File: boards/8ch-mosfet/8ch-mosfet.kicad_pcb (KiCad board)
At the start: 2 copper layers, 184 x 136 mm, 146 parts, among them J1 N2K, J10 Screw_Terminal_01x02, J11 Screw_Terminal_01x02, J12 Screw_Terminal_01x02, J2 I2C, J3 Screw_Terminal_01x09, J5 Screw_Terminal_01x02, J6 Screw_Terminal_01x02, J7 Screw_Terminal_01x02, J8 Screw_Terminal_01x02, J9 Screw_Terminal_01x02, M1 Fan_4pin, Q1 BC817, Q10 IRF4905, Q11 BC817, Q12 IRF4905, Q13 BC817, Q14 IRF4905, Q15 BC817, Q16 IRF4905, Q2 IRF4905, Q3 BC817, Q4 IRF4905, Q5 BC817, Q6 IRF4905, Q7 BC817, Q8 IRF4905, Q9 BC817, U1 ESP32-DEVKITC, U10 ACS725xLCTR-20AU, U11 ACS725xLCTR-20AU, U12 ACS725xLCTR-20AU, U2 MCP3208, U3 R-78B3.3-2.0, U5 ACS725xLCTR-20AU, U6 ACS725xLCTR-20AU, U7 ACS725xLCTR-20AU, U8 ACS725xLCTR-20AU, U9 ACS725xLCTR-20AU

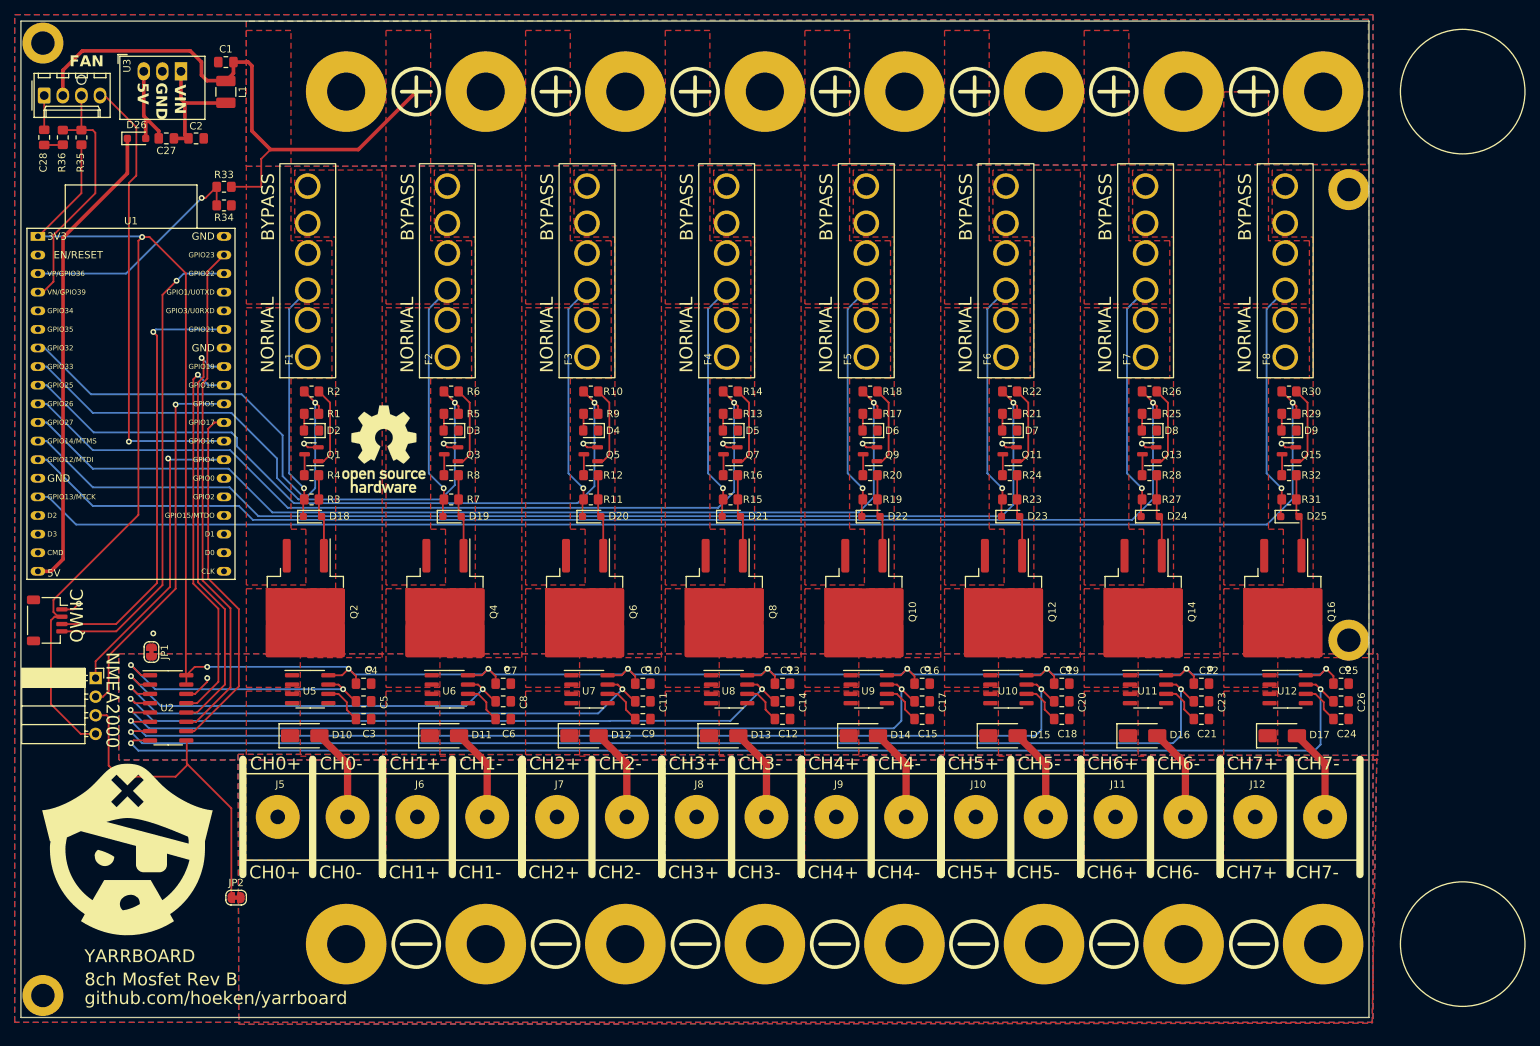
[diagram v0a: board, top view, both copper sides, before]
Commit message: changed ground connectors and updated busbar positions.
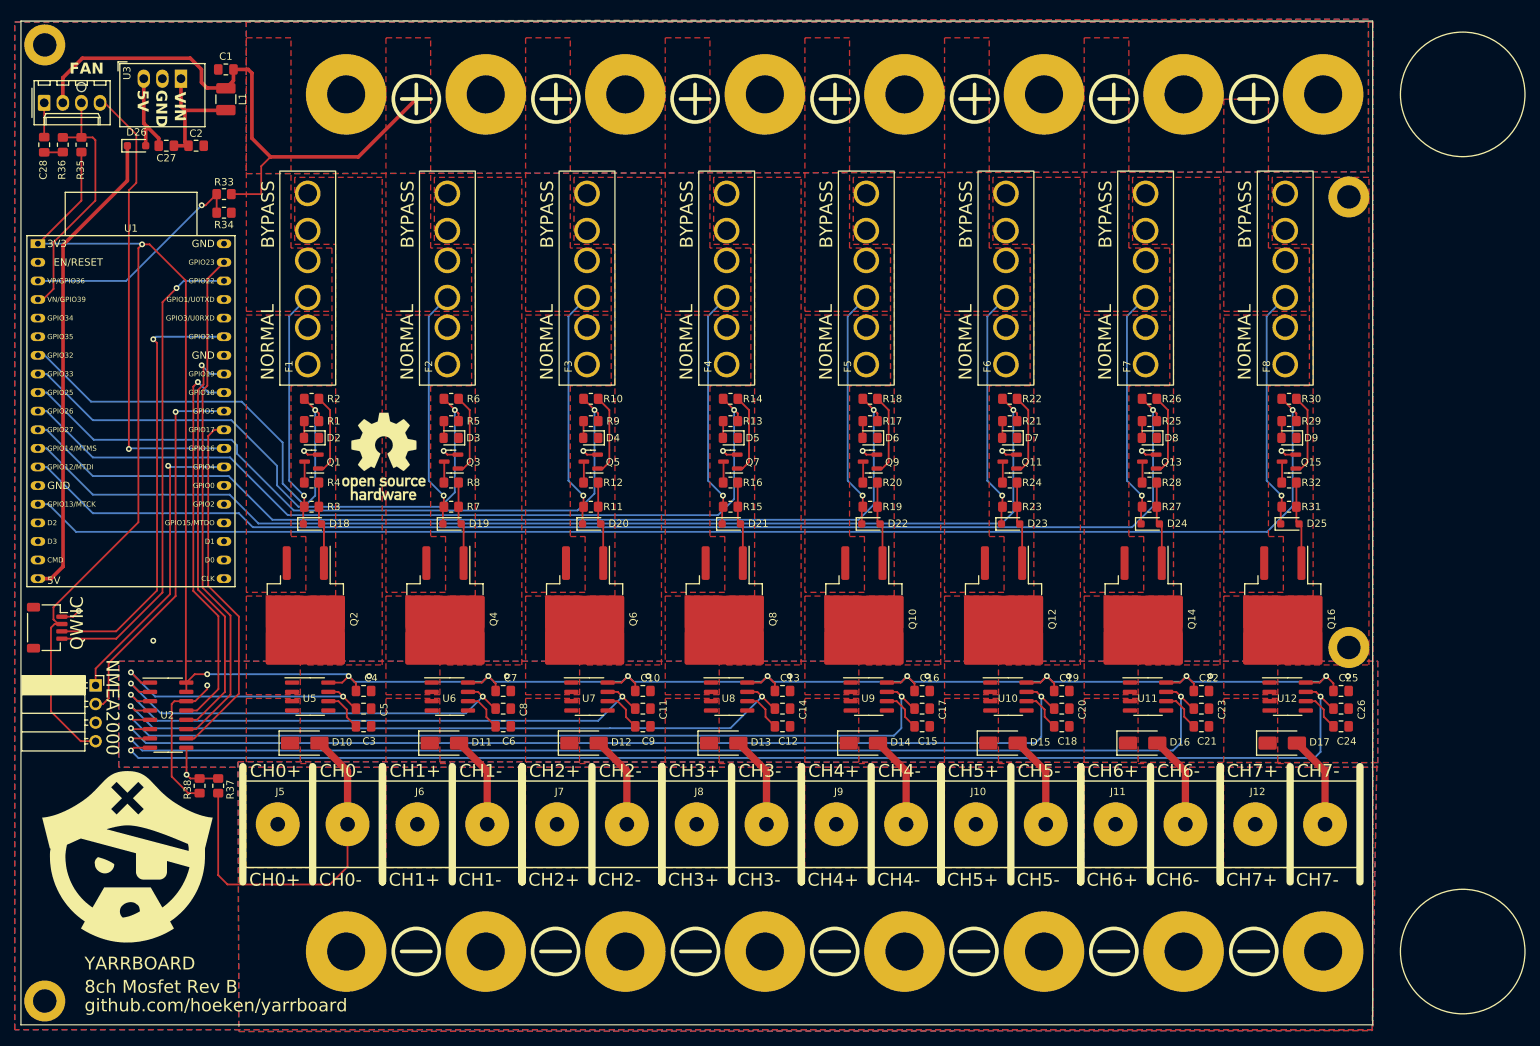
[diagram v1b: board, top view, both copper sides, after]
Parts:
- removed JP1, JP2: SolderJumper_2_Bridged, Jumper:SolderJumper-2_P1.3mm_Bridged_RoundedPad1.0x1.5mm
- added R37: 0R, Resistor_SMD:R_0805_2012Metric_Pad1.20x1.40mm_HandSolder, F.Cu at (26.9, 104.4)
- added R38: 0R, Resistor_SMD:R_0805_2012Metric_Pad1.20x1.40mm_HandSolder, F.Cu at (24.4, 104.4)
- moved locked 1.02 mm to (206.3, 127.0)
- moved C1 1.00 mm to (28.0, 6.60)
- moved C10 1.00 mm to (84.9, 91.4)
- moved C11 1.00 mm to (84.9, 93.8)
- moved C12 1.00 mm to (103.9, 96.3)
- moved C13 1.00 mm to (103.9, 91.4)
- moved C14 1.00 mm to (103.9, 93.8)
- moved C15 1.00 mm to (123.0, 96.3)
- moved C16 1.00 mm to (123.0, 91.4)
- moved C17 1.00 mm to (123.0, 93.8)
- moved C18 1.00 mm to (142.1, 96.3)
- moved C19 1.00 mm to (142.1, 91.4)
- moved C2 1.00 mm to (23.9, 17.0)
- moved C20 1.00 mm to (142.1, 93.8)
- moved C21 1.00 mm to (161.1, 96.3)
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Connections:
- C27 pad 2: Net-(D26-A) -> +5V
- D26 pad 1: +5V -> Net-(D26-K)
- D26 pad 2: Net-(D26-A) -> +5V
- U1 pad 19: +5V -> Net-(D26-K)
- U3 pad 3: Net-(D26-A) -> +5V
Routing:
- net Net-(D26-K): track 0.00 -> 65.2 mm
- net +5V: track 65.2 -> 12.6 mm
- net GNDD: track 69.2 -> 32.9 mm, vias 10 -> 11
- net GNDPWR: track 101.4 -> 137.5 mm
- net GNDA: track 4.23 -> 21.0 mm
- net Net-(D26-A): track 12.6 -> 0.00 mm
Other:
- board size 184 x 136 mm -> 184.5 x 137 mm

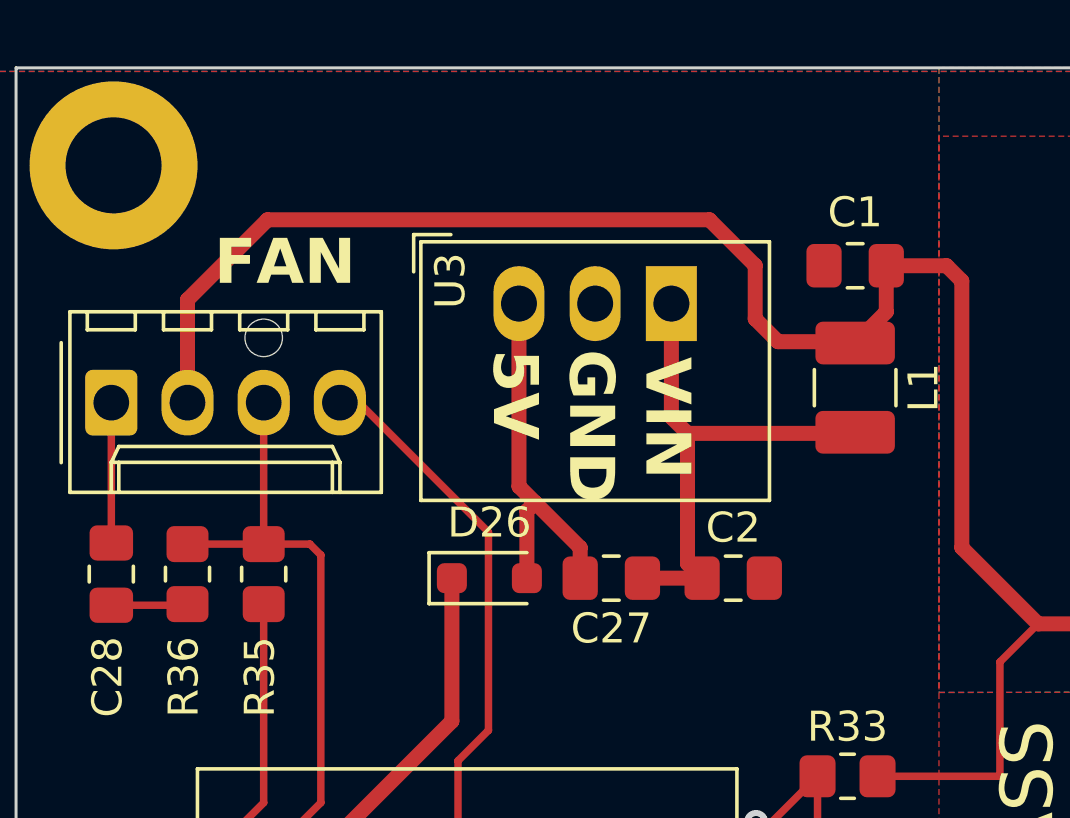
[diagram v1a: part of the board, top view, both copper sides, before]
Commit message: updated footprints, changed 5v diode, and added jumpers for fan voltage
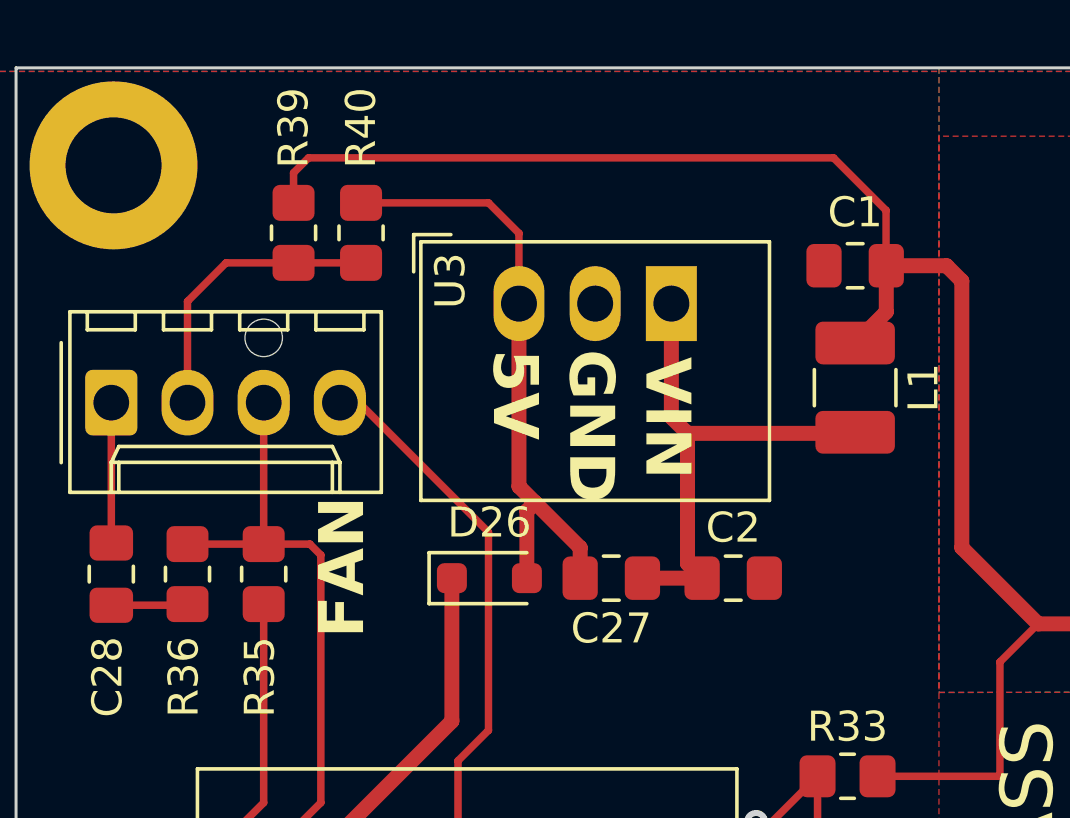
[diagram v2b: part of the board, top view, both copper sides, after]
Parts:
- added R39: 0R, Resistor_SMD:R_0805_2012Metric_Pad1.20x1.40mm_HandSolder, F.Cu at (9.25, 5.50)
- added R40: 0R, Resistor_SMD:R_0805_2012Metric_Pad1.20x1.40mm_HandSolder, F.Cu at (11.5, 5.50)
- D26: value BZX384 -> CMHSH5-2L
- J3, locked: value Screw_Terminal_01x09 -> Screw_Terminal_01x08
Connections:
- M1 pad 2: +24V -> Net-(M1-+)
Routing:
- net Net-(M1-+): track 0.00 -> 9.69 mm
- net +5V: track 12.6 -> 20.7 mm
- net +24V: track 345.5 -> 339.5 mm

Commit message: mosfet driver resistors updated, looking good now.
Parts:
- R11, R15, R19, R23, R27, R3, R31, R7: value 22k -> 100K
- R12, R16, R20, R24, R28, R32, R4, R8: value 4.7k -> 22K
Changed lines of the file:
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@@
         (effects (font (size 1 1) (thickness 0.15)))
     )
-    (fp_text value "22k" (at 0 1.65) (layer "F.Fab")
+    (fp_text value "100K" (at 0 1.65) (layer "F.Fab")
         (effects (font (size 1 1) (thickness 0.15)))
     )
@@
         (effects (font (size 1 1) (thickness 0.15)))
     )
-    (fp_text value "22k" (at 0 1.65) (layer "F.Fab")
+    (fp_text value "100K" (at 0 1.65) (layer "F.Fab")
         (effects (font (size 1 1) (thickness 0.15)))
     )
@@
         (effects (font (size 1 1) (thickness 0.15)))
     )
-    (fp_text value "4.7k" (at 0 1.65) (layer "F.Fab")
+    (fp_text value "22K" (at 0 1.65) (layer "F.Fab")
         (effects (font (size 1 1) (thickness 0.15)))
     )
@@
         (effects (font (size 1 1) (thickness 0.15)))
     )
-    (fp_text value "4.7k" (at 0 1.65) (layer "F.Fab")
+    (fp_text value "22K" (at 0 1.65) (layer "F.Fab")
         (effects (font (size 1 1) (thickness 0.15)))
     )
@@
         (effects (font (size 1 1) (thickness 0.15)))
     )
-    (fp_text value "4.7k" (at 0 1.65) (layer "F.Fab")
+    (fp_text value "22K" (at 0 1.65) (layer "F.Fab")
         (effects (font (size 1 1) (thickness 0.15)))
     )
@@
         (effects (font (size 1 1) (thickness 0.15)))
     )
-    (fp_text value "4.7k" (at 0 1.65) (layer "F.Fab")
+    (fp_text value "22K" (at 0 1.65) (layer "F.Fab")
         (effects (font (size 1 1) (thickness 0.15)))
     )
@@
         (effects (font (size 1 1) (thickness 0.15)))
     )
-    (fp_text value "4.7k" (at 0 1.65) (layer "F.Fab")
+    (fp_text value "22K" (at 0 1.65) (layer "F.Fab")
         (effects (font (size 1 1) (thickness 0.15)))
     )
@@
     (property "Sheetname" "")
     (property "Vendor" " 652-CR0805JW-102ELF ")
+    (property "dnp" "")
     (property "ki_description" "Resistor, small US symbol")
     (property "ki_keywords" "r resistor")
@@
         (effects (font (size 1 1) (thickness 0.15)))
     )
-    (fp_text value "22k" (at 0 1.65) (layer "F.Fab")
+    (fp_text value "100K" (at 0 1.65) (layer "F.Fab")
         (effects (font (size 1 1) (thickness 0.15)))
     )
@@
         (effects (font (size 1 1) (thickness 0.15)))
     )
-    (fp_text value "22k" (at 0 1.65) (layer "F.Fab")
+    (fp_text value "100K" (at 0 1.65) (layer "F.Fab")
         (effects (font (size 1 1) (thickness 0.15)))
     )
@@
         (effects (font (size 1 1) (thickness 0.15)))
     )
-    (fp_text value "22k" (at 0 1.65) (layer "F.Fab")
+    (fp_text value "100K" (at 0 1.65) (layer "F.Fab")
         (effects (font (size 1 1) (thickness 0.15)))
     )
@@
         (effects (font (size 1 1) (thickness 0.15)))
     )
-    (fp_text value "22k" (at 0 1.65) (layer "F.Fab")
+    (fp_text value "100K" (at 0 1.65) (layer "F.Fab")
         (effects (font (size 1 1) (thickness 0.15)))
     )
@@
         (effects (font (size 1 1) (thickness 0.15)))
     )
-    (fp_text value "22k" (at 0 1.65) (layer "F.Fab")
+    (fp_text value "100K" (at 0 1.65) (layer "F.Fab")
         (effects (font (size 1 1) (thickness 0.15)))
     )
@@
         (effects (font (size 1 1) (thickness 0.15)))
     )
-    (fp_text value "4.7k" (at 0 1.65) (layer "F.Fab")
+    (fp_text value "22K" (at 0 1.65) (layer "F.Fab")
         (effects (font (size 1 1) (thickness 0.15)))
     )
@@
         (effects (font (size 1 1) (thickness 0.15)))
     )
-    (fp_text value "4.7k" (at 0 1.65) (layer "F.Fab")
+    (fp_text value "22K" (at 0 1.65) (layer "F.Fab")
         (effects (font (size 1 1) (thickness 0.15)))
     )
@@
         (effects (font (size 1 1) (thickness 0.15)))
     )
-    (fp_text value "22k" (at 0 1.65) (layer "F.Fab")
+    (fp_text value "100K" (at 0 1.65) (layer "F.Fab")
         (effects (font (size 1 1) (thickness 0.15)))
     )
@@
         (effects (font (size 1 1) (thickness 0.15)))
     )
-    (fp_text value "4.7k" (at 0 1.65) (layer "F.Fab")
+    (fp_text value "22K" (at 0 1.65) (layer "F.Fab")
         (effects (font (size 1 1) (thickness 0.15)))
     )
